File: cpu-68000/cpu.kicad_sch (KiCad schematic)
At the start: 23 parts, among them U104 74HC05, U301 MC68000FN, U302 74HC2G08DC, U303 TL7733B, U304 74HC175, U305 ATF22V10C, U306 74HC148

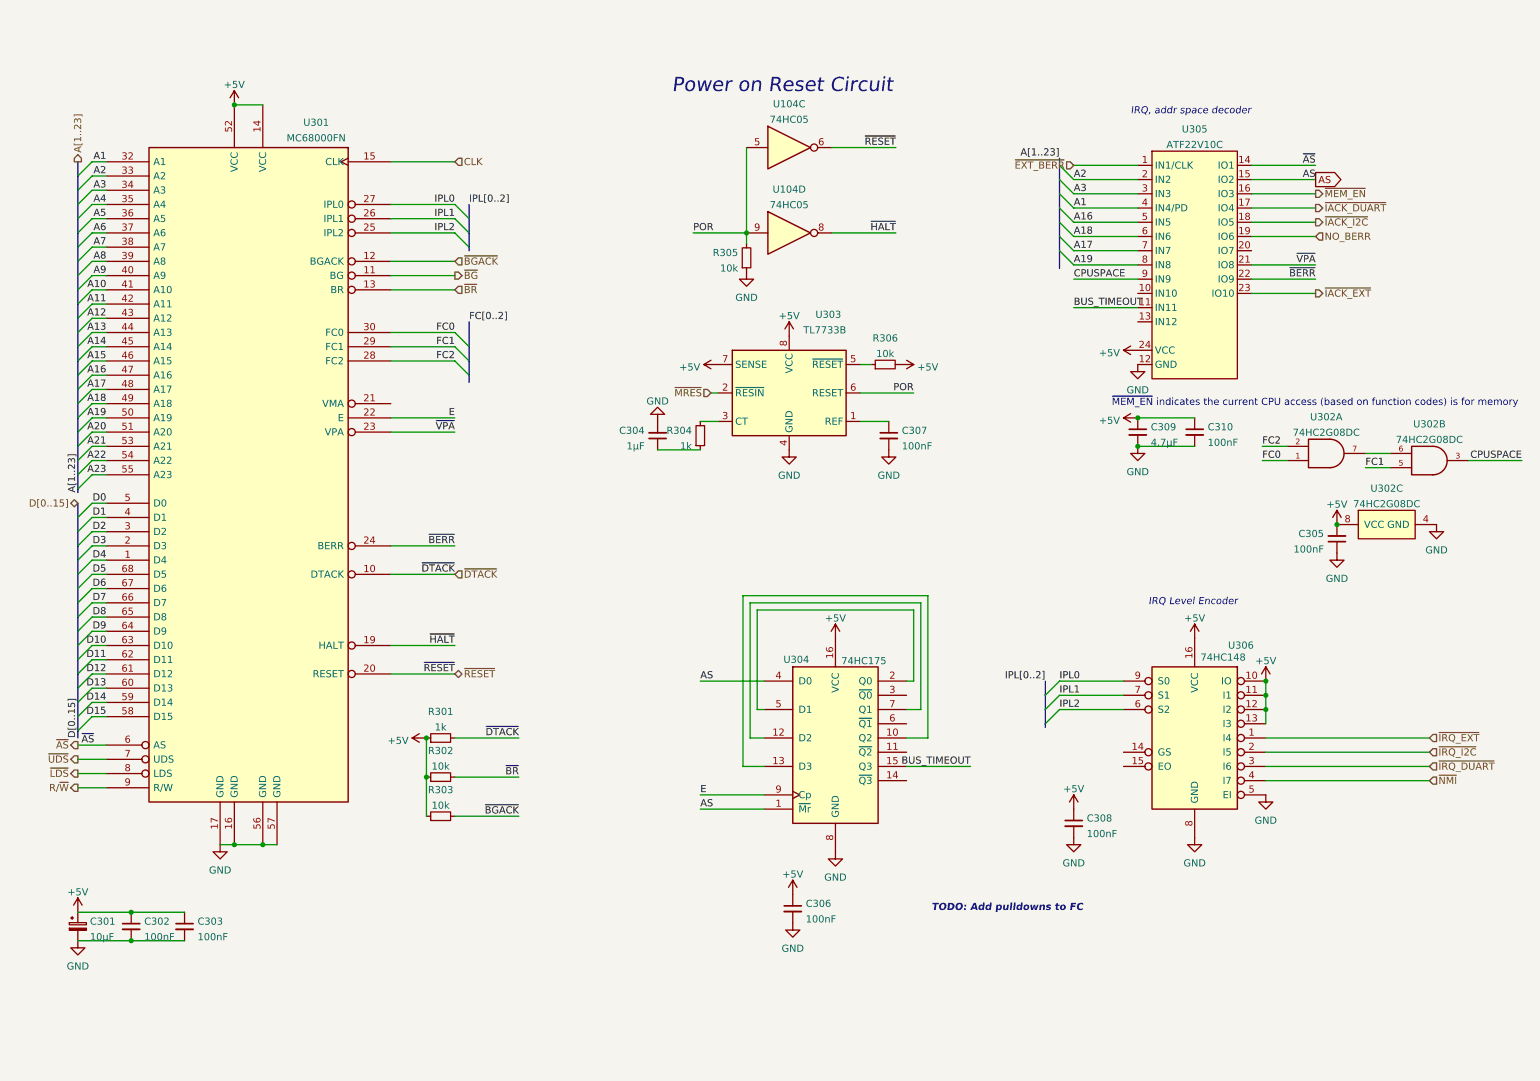
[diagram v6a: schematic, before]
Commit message: More control signals; start RAM routing
- Started routing the address/data bus for the RAM, including some
  rejigging of the data bus layout

- Added a fuse and power conditioning for 12V, to be used for the analog
  section on the sound side
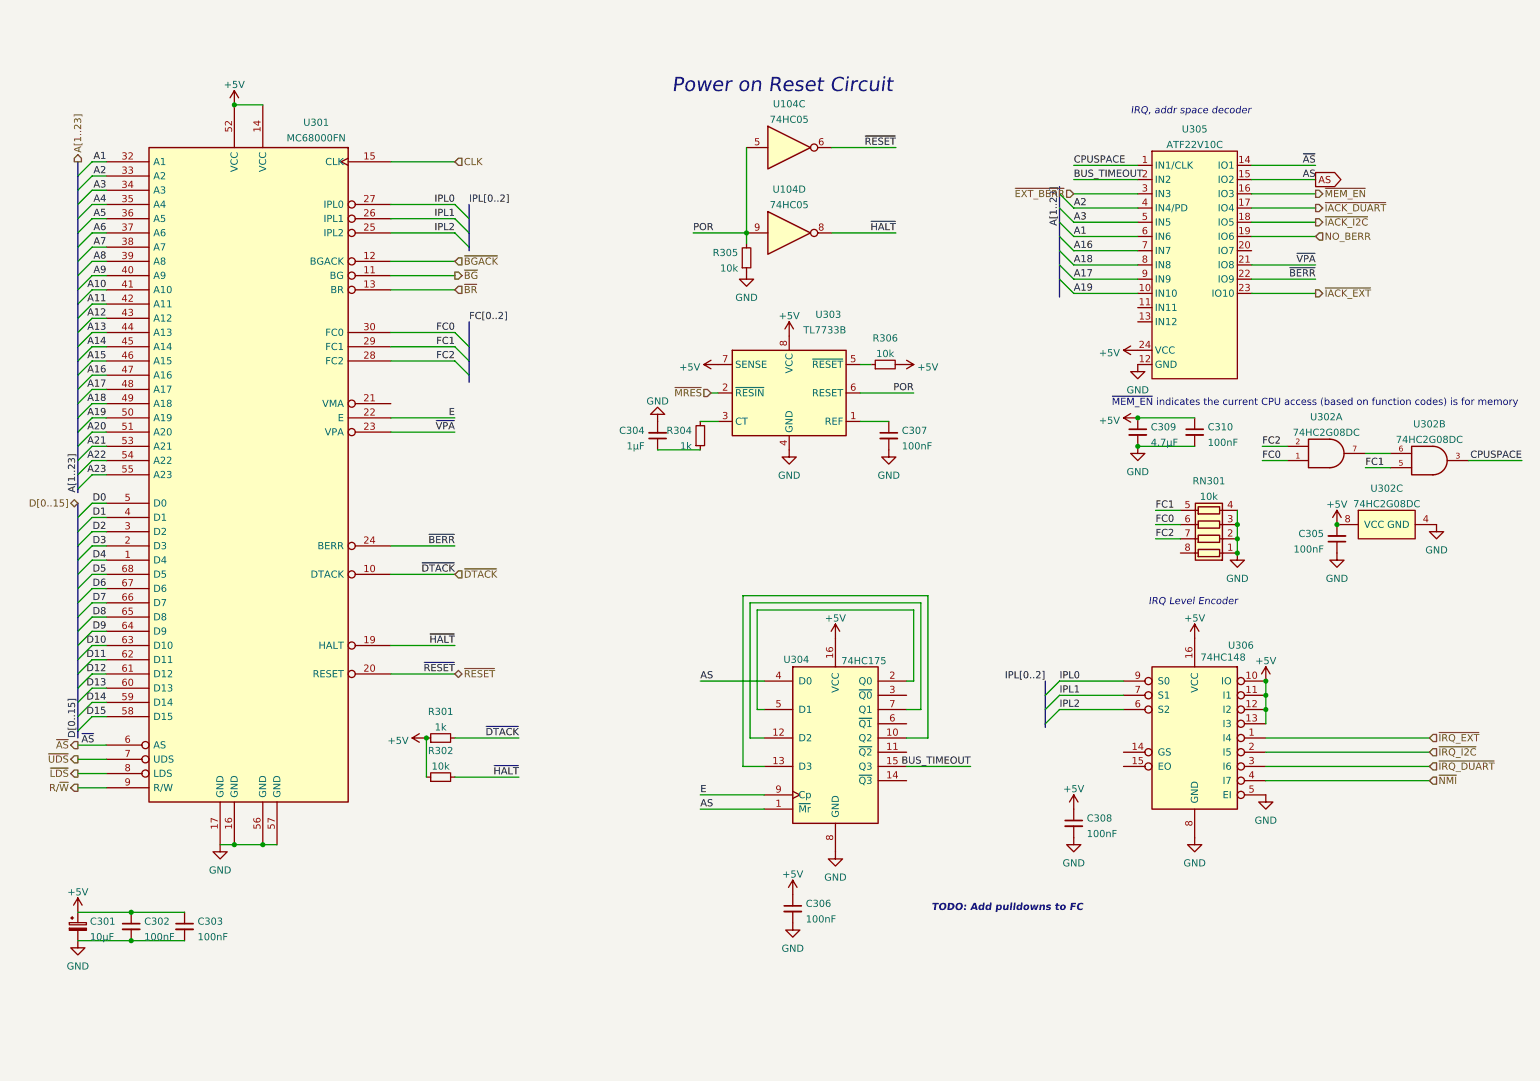
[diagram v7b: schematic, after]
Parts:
- removed R303: 10k, Resistor_SMD:R_0805_2012Metric, symbol Device:R_Small
- added RN301: 10k, Resistor_SMD:R_Array_Convex_4x1206, symbol Device:R_Pack04
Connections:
- net A1: now also U305.6 (IN6); no longer U305.4 (IN4/PD)
- net A16: now also U305.7 (IN7); no longer U305.5 (IN5)
- net A17: now also U305.9 (IN9); no longer U305.7 (IN7)
- net A18: now also U305.8 (IN8); no longer U305.6 (IN6)
- net A19: now also U305.10 (IN10); no longer U305.8 (IN8)
- net A2: now also U305.4 (IN4/PD); no longer U305.2 (IN2)
- net A3: now also U305.5 (IN5); no longer U305.3 (IN3)
- net BUS_TIMEOUT: now also U305.2 (IN2); no longer U305.11 (IN11)
- net CPUSPACE: now also U305.1 (IN1/CLK); no longer U305.9 (IN9)
- net FC0: now also RN301.6 (R3.2)
- net FC1: now also RN301.5 (R4.2)
- net FC2: now also RN301.7 (R2.2)
- net GND: now also RN301.1 (R1.1), RN301.2 (R2.1), RN301.3 (R3.1), RN301.4 (R4.1)
- net ~{BR}: no longer R302.2
- net ~{EXT_BERR}: now also U305.3 (IN3); no longer U305.1 (IN1/CLK)
- net ~{HALT}: now also R302.2
